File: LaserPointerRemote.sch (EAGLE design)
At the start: 34 parts, among them IC1 MEGA8-AI, IC2 MCP1640, J1 AVR_SPI_PRG_6NS, U1 2N7002, X1 22-05-7028-02, X3 22-23-2031

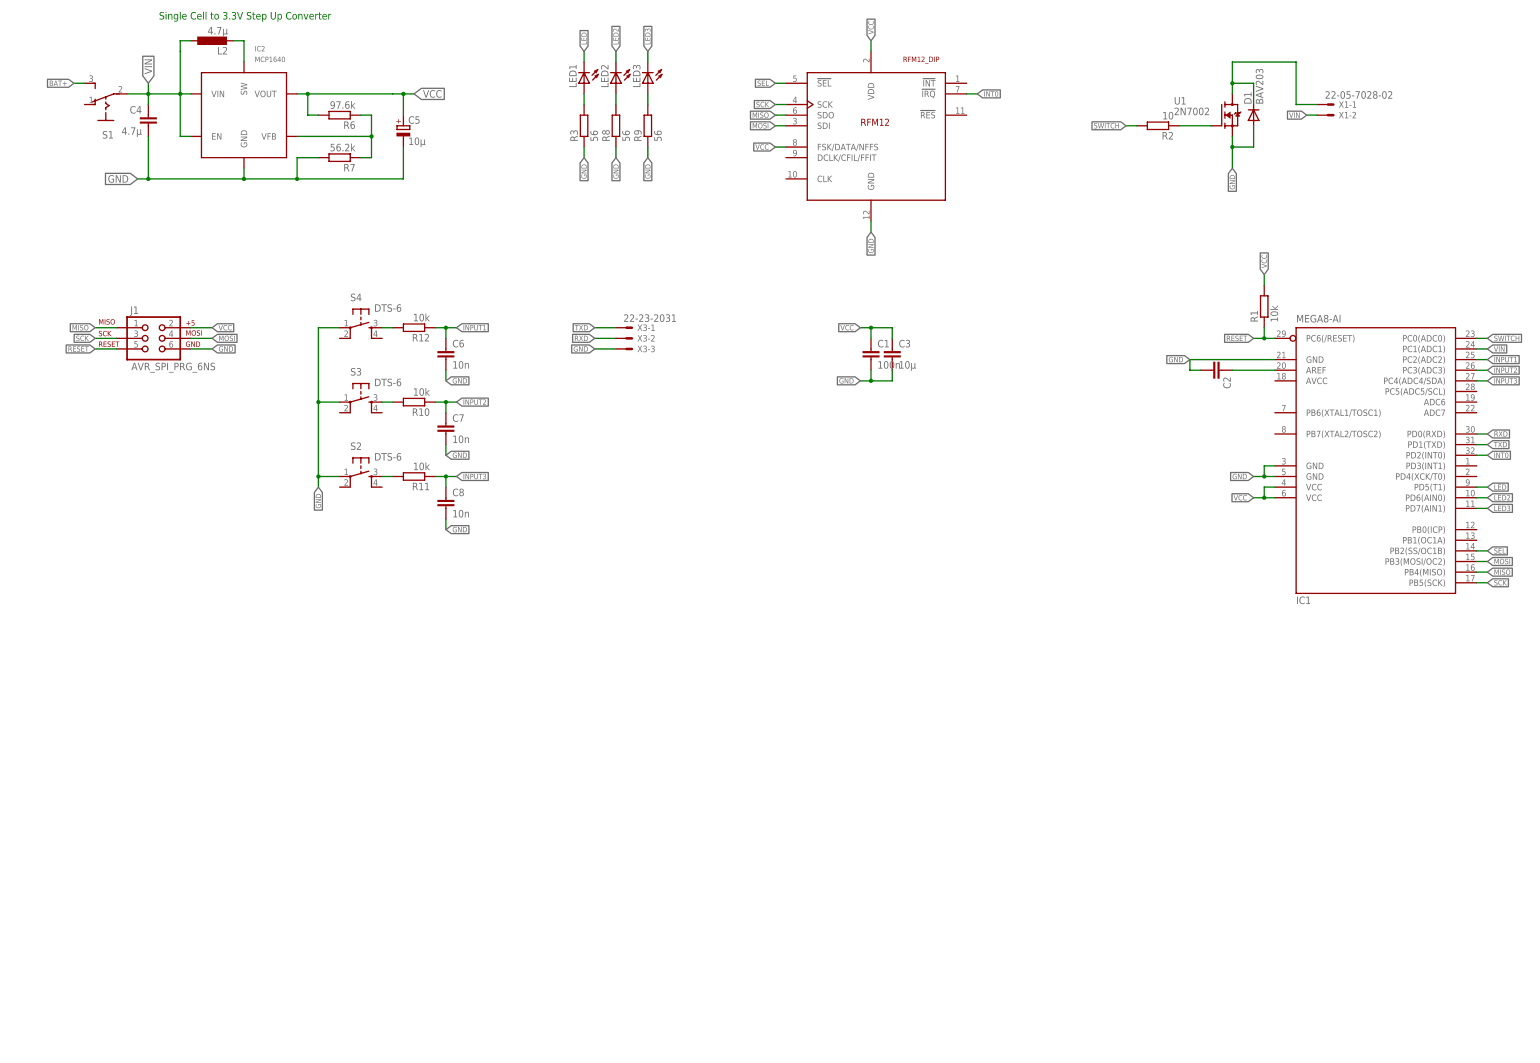
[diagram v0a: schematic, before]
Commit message: Refactored PCB to fit the strapupox
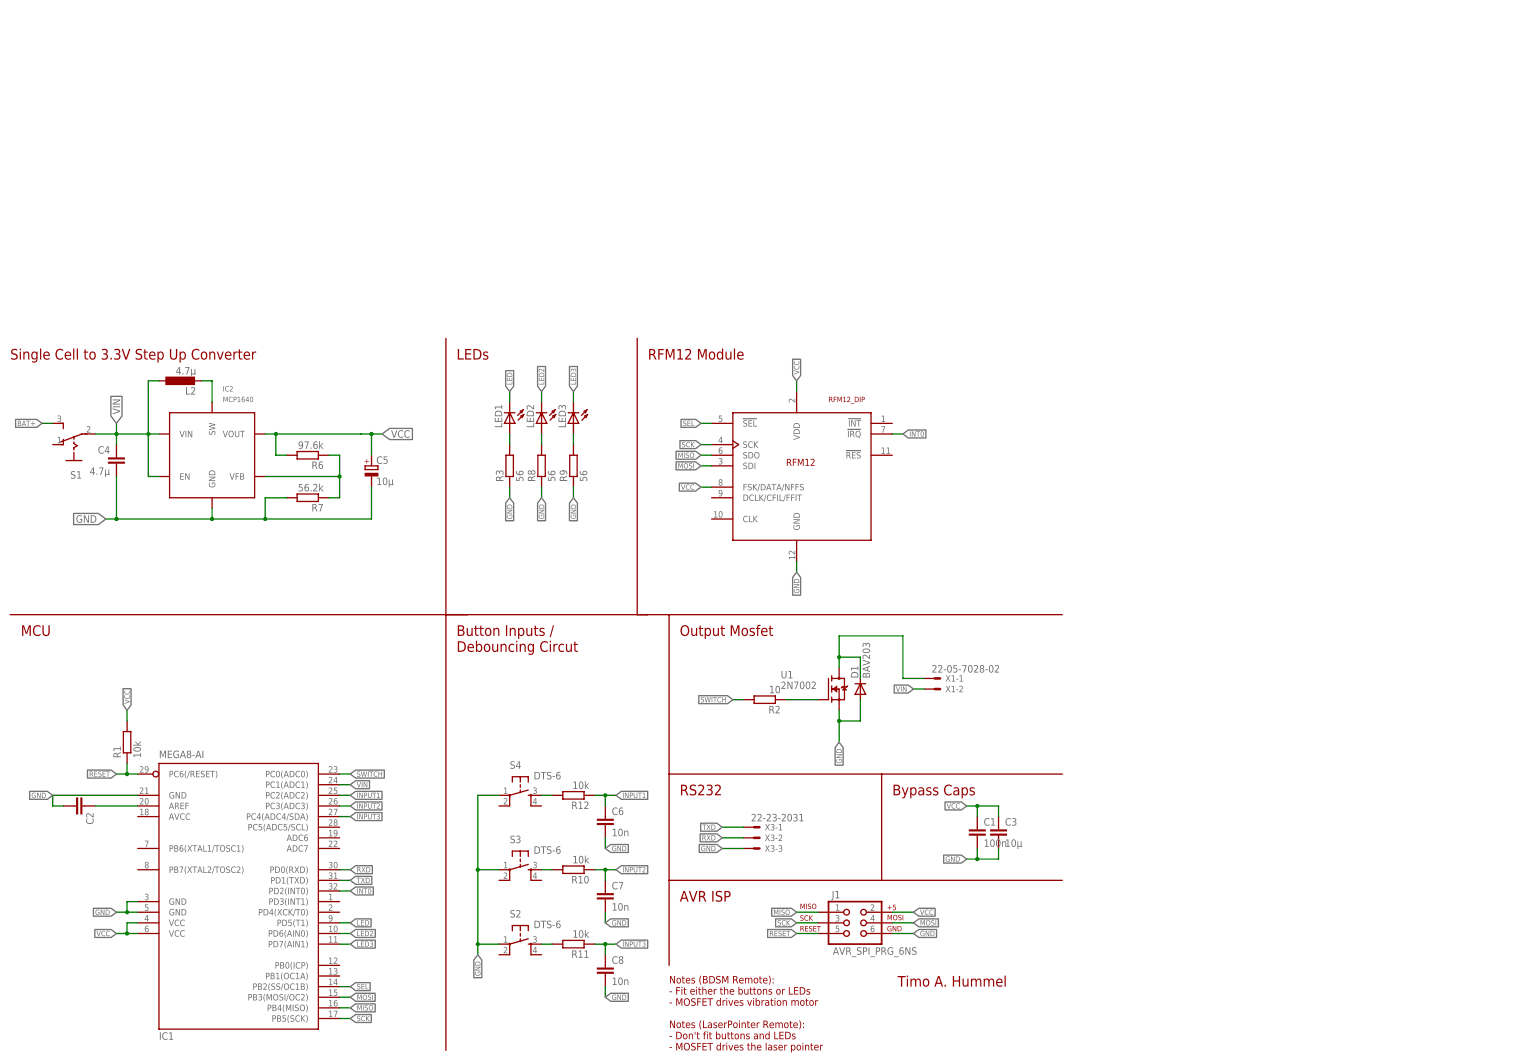
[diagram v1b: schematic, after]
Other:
- note added: "AVR ISP"
- note added: "Button Inputs / Debouncing Circut"
- note added: "Bypass Caps"
- note added: "LEDs"
- note added: "MCU"
- note added: "Notes (BDSM Remote): - Fit either the buttons or LEDs - MOSFET drives vibration motor Notes (LaserPointer Remote): - Don't fit buttons and LEDs - MOSFET drives the laser pointer"
- note added: "Output Mosfet"
- note added: "RFM12 Module"
- note added: "RS232"
- note added: "Timo A. Hummel"
- moved on the sheet: C1, C2, C3, C4, C5, C6, C7, C8, D1, IC1, IC2, J1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

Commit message: Changed VCC to 5V instead of 3.3V Added NPN transistor instead of mosfet Connected AVCC
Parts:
- removed U1: 2N7002, SteveMarple:2N7002
- removed X1: 22-05-7028-02, con-molex:22-05-7028-02
- removed X3: 22-23-2031, con-molex:22-23-2031
- added JP1: (no value), pinhead:PINHD-1X2
- added JP2: (no value), pinhead:PINHD-1X3
- added T1: BC818, transistor:BC818-16-NPN-SOT23-BEC
- R6: value 97.6k -> 100k
- R7: value 56.2k -> 33k
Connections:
- net GND: now also JP2.3, T1.E; no longer U1.S, X3-3.S
- net N$1: now also T1.B; no longer U1.G
- net N$2: now also JP1.1, T1.C; no longer U1.D, X1-1.S
- net RXD: now also JP2.2; no longer X3-2.S
- net TXD: now also JP2.1; no longer X3-1.S
- net VCC: now also IC1.AVCC
- net VIN: now also JP1.2; no longer IC1.PC1(ADC1), X1-2.S
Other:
- note added: "Output Transistor"
- note added: "Single Cell to 5V Step Up Converter (the RFM12 module is a bit picky, so no 3.3V)"
- note removed: "Output Mosfet"
- note removed: "Single Cell to 3.3V Step Up Converter"
- moved on the sheet: C4, C5, IC2, L2, R2, R6, R7, S1

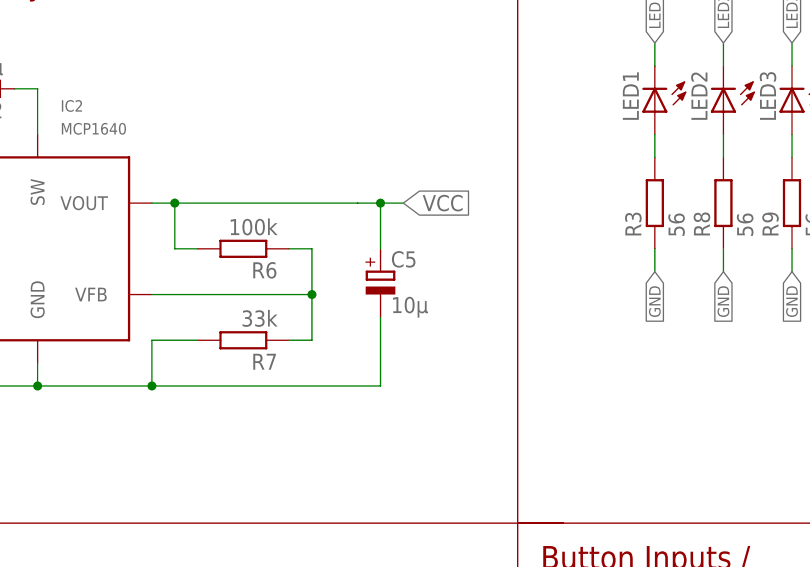
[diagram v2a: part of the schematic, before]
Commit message: Use X7R output cap instead of a tantalum one
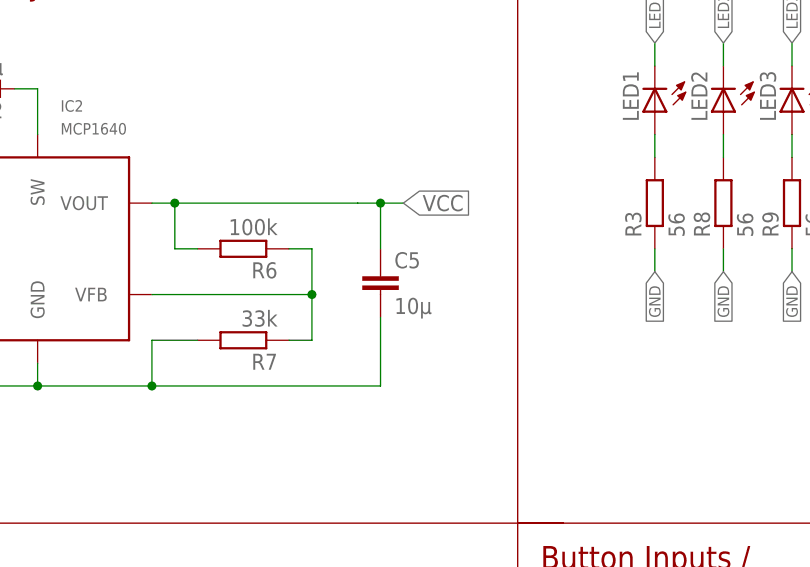
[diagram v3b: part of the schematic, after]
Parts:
- C5: device rcl:CPOL-EUC/6032-28R -> rcl:C-EUC0805
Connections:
- net GND: now also C5.2; no longer C5.-
- net VCC: now also C5.1; no longer C5.+
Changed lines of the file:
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@@
 <attribute name="OC_TME" value="CRCW080556K2FKTABC"/>
 </part>
-<part name="C5" library="rcl" deviceset="CPOL-EU" device="C/6032-28R" value="10µ"/>
+<part name="C5" library="rcl" deviceset="C-EU" device="C0805" value="10µ"/>
 <part name="S2" library="switch-tact" deviceset="DTS-6" device=""/>
 <part name="S3" library="switch-tact" deviceset="DTS-6" device=""/>
@@
 <wire x1="68.58" y1="124.46" x2="55.88" y2="124.46" width="0.1524" layer="91"/>
 <junction x="55.88" y="124.46"/>
-<pinref part="C5" gate="G$1" pin="-"/>
+<pinref part="C5" gate="G$1" pin="2"/>
 <wire x1="68.58" y1="124.46" x2="93.98" y2="124.46" width="0.1524" layer="91"/>
 <wire x1="93.98" y1="124.46" x2="93.98" y2="132.08" width="0.1524" layer="91"/>
@@
 <wire x1="71.12" y1="144.78" x2="91.44" y2="144.78" width="0.1524" layer="91"/>
 <junction x="71.12" y="144.78"/>
-<pinref part="C5" gate="G$1" pin="+"/>
+<pinref part="C5" gate="G$1" pin="1"/>
 <wire x1="93.98" y1="139.7" x2="93.98" y2="144.78" width="0.1524" layer="91"/>
 <wire x1="93.98" y1="144.78" x2="91.44" y2="144.78" width="0.1524" layer="91"/>
